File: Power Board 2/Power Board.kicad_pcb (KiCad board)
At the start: 4 copper layers, 191 parts, among them IC1 LTC4151IMS#PBF, IC2 LTC4151IMS#PBF, J1 Conn_01x02, J18 Conn_02x03_Top_Bottom, J19 Conn_01x02, J2 Conn_01x02, J21 Conn_01x02, J3 Conn_01x02, J4 Conn_01x02, J5 Conn_01x02, J6 Conn_01x02, J7 Conn_01x02, J8 Conn_01x02, J9 Conn_02x03_Top_Bottom, Q1 Q_PMOS_GDS, Q10 Q_NMOS_GDS, Q11 Q_NMOS_GDS, Q12 Q_NMOS_GDS, Q13 Q_NMOS_GDS, Q14 Q_NMOS_GDS, Q15 Q_NMOS_GDS, Q16 Q_NMOS_GDS, Q17 Q_NMOS_GDS, Q18 Q_NMOS_GDS, Q19 Q_NMOS_GDS, Q2 Q_PMOS_GDS, Q20 Q_NMOS_GDS, Q21 Q_NMOS_GDS, Q22 Q_NMOS_GDS, Q3 Q_PMOS_GDS, Q4 Q_PMOS_GDS, Q5 Q_PMOS_GDS, Q6 Q_PMOS_GDS, Q7 Q_PMOS_GDS, Q8 Q_PMOS_GDS, Q9 Q_NMOS_GDS, U1 LTC4372CDD-PBF, U10 ACS770xCB-050U-PFF, U11 ACS770xCB-050U-PFF, U12 ACS770xCB-050U-PFF, U13 ACS770xCB-050U-PFF, U14 ACS770xCB-050U-PFF, U15 ADC128S052CIMT, U17 TLV70033_SOT23-5, U2 LTC4372CDD-PBF, U3 LTC4372CDD-PBF, U4 LTC4372CDD-PBF, U5 LTC4372CDD-PBF, U6 LTC4372CDD-PBF, U7 LTC4372CDD-PBF, U8 ACS770xCB-050U-PFF, U9 ACS770xCB-050U-PFF

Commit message: added mounting holes
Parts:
- added H29: MountingHole_Pad, MountingHole:MountingHole_3.2mm_M3_DIN965, F.Cu at (149.5, 113.8)
- moved H5 0.08 mm to (52.9, 113.8)
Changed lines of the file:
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@@
 		(embedded_fonts no)
 	)
+	(footprint "MountingHole:MountingHole_3.2mm_M3_DIN965"
+		(layer "F.Cu")
+		(at 149.463953 113.821117)
+		(descr "Mounting Hole 3.2mm, M3, no annular, generated by kicad-footprint-generator mountinghole.py")
+		(tags "mountinghole M3 DIN965")
+		(property "Reference" "H29"
+			(at 3.425657 -2.784012 0)
+			(layer "F.SilkS")
+			(effects
+				(font
+					(size 1 1)
+					(thickness 0.15)
+				)
+			)
+		)
+		(property "Value" "MountingHole_Pad"
+			(at 0 3.75 0)
+			(layer "F.Fab")
+			(effects
+				(font
+					(size 1 1)
+					(thickness 0.15)
+				)
+			)
+		)
+		(property "Datasheet" "~"
+			(at 0 0 0)
+			(layer "F.Fab")
+			(hide yes)
+			(effects
+				(font
+					(size 1.27 1.27)
+					(thickness 0.15)
+				)
+			)
+		)
+		(property "Description" "Mounting Hole without connection"
+			(at 0 0 0)
+			(layer "F.Fab")
+			(hide yes)
+			(effects
+				(font
+					(size 1.27 1.27)
+					(thickness 0.15)
+				)
+			)
+		)
+		(attr exclude_from_pos_files exclude_from_bom)
+		(fp_circle
+			(center 0 0)
+			(end 2.8 0)
+			(stroke
+				(width 0.15)
+				(type solid)
+			)
+			(fill no)
+			(layer "Cmts.User")
+		)
+		(fp_circle
+			(center 0 0)
+			(end 3.05 0)
+			(stroke
+				(width 0.05)
+				(type solid)
+			)
+			(fill no)
+			(layer "F.CrtYd")
+		)
+		(fp_text user "${REFERENCE}"
+			(at 0 0 0)
+			(layer "F.Fab")
+			(effects
+				(font
+					(size 1 1)
+					(thickness 0.15)
+				)
+			)
+		)
+		(pad "" np_thru_hole circle
+			(at 0 0)
+			(size 3.2 3.2)
+			(drill 3.2)
+			(layers "*.Cu" "*.Mask")
+		)
+		(embedded_fonts no)
+	)
 	(footprint "Capacitor_SMD:C_0603_1608Metric"
 		(layer "F.Cu")
@@
 	(footprint "MountingHole:MountingHole_3.2mm_M3_DIN965"
 		(layer "F.Cu")
-		(at 52.785 113.821117)
+		(at 52.863953 113.821117)
 		(descr "Mounting Hole 3.2mm, M3, no annular, generated by kicad-footprint-generator mountinghole.py")
 		(tags "mountinghole M3 DIN965")

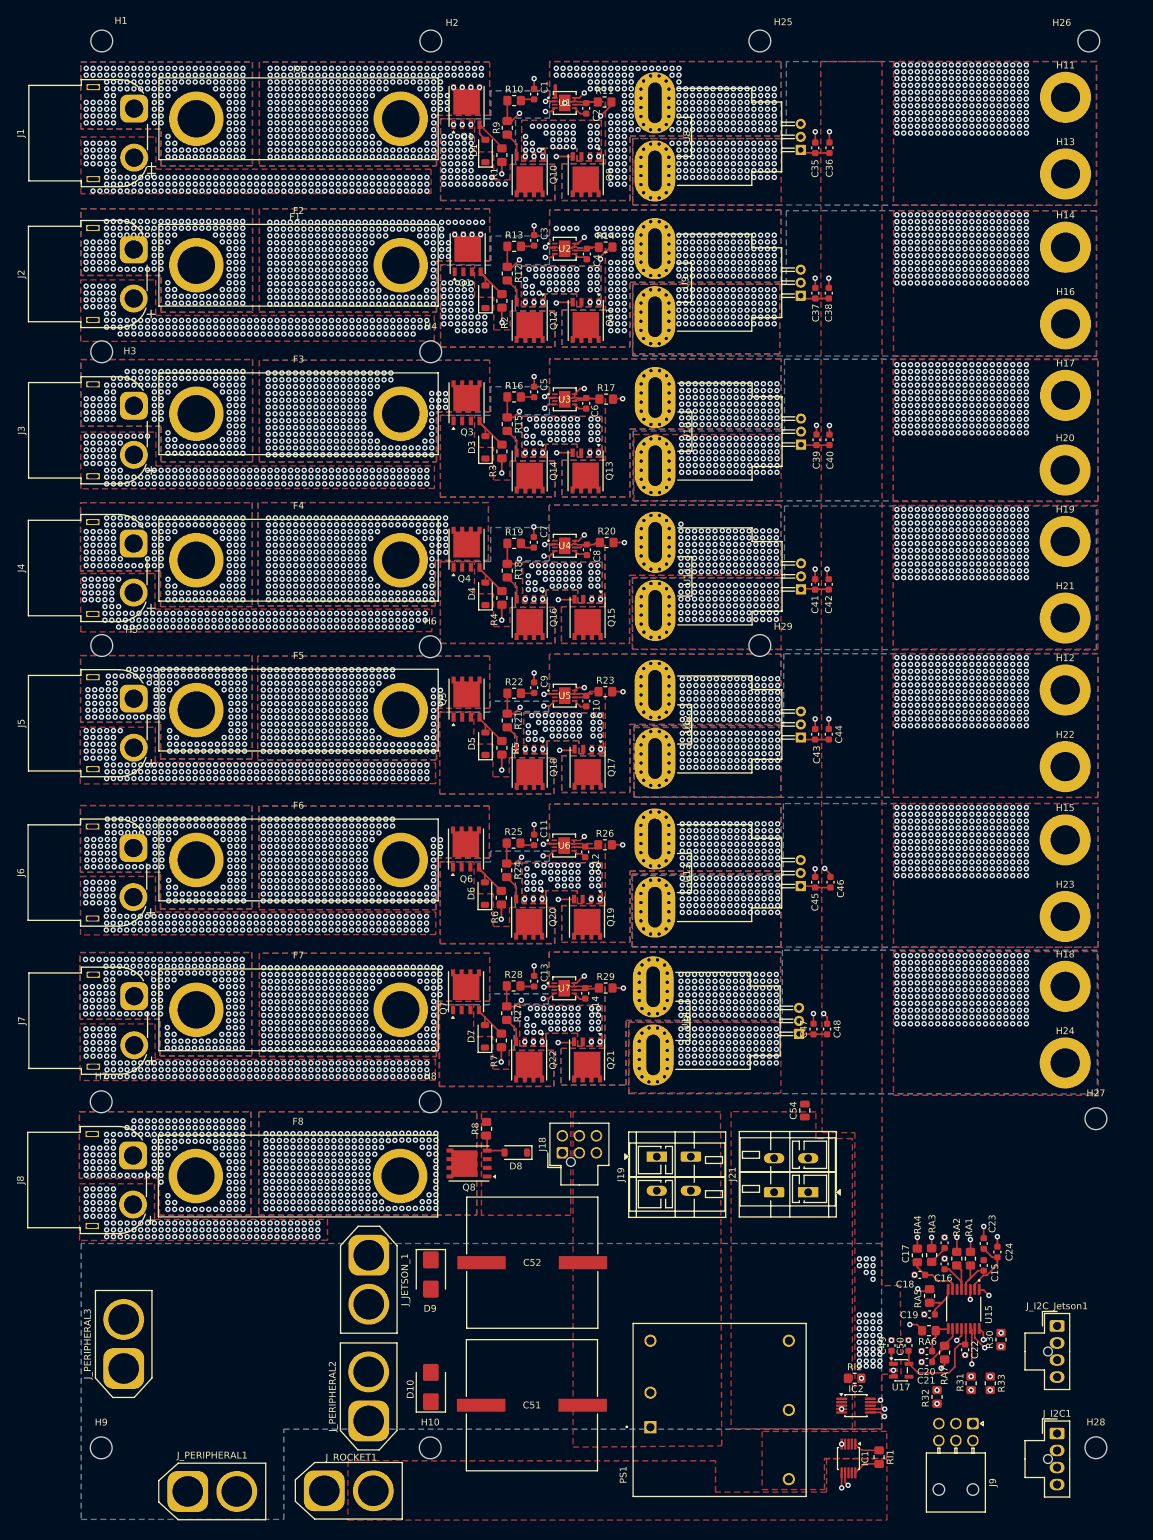
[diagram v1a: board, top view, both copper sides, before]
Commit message: minor updates to BMS; edge cuts, GND pour, via stitching, missed connections for PDB
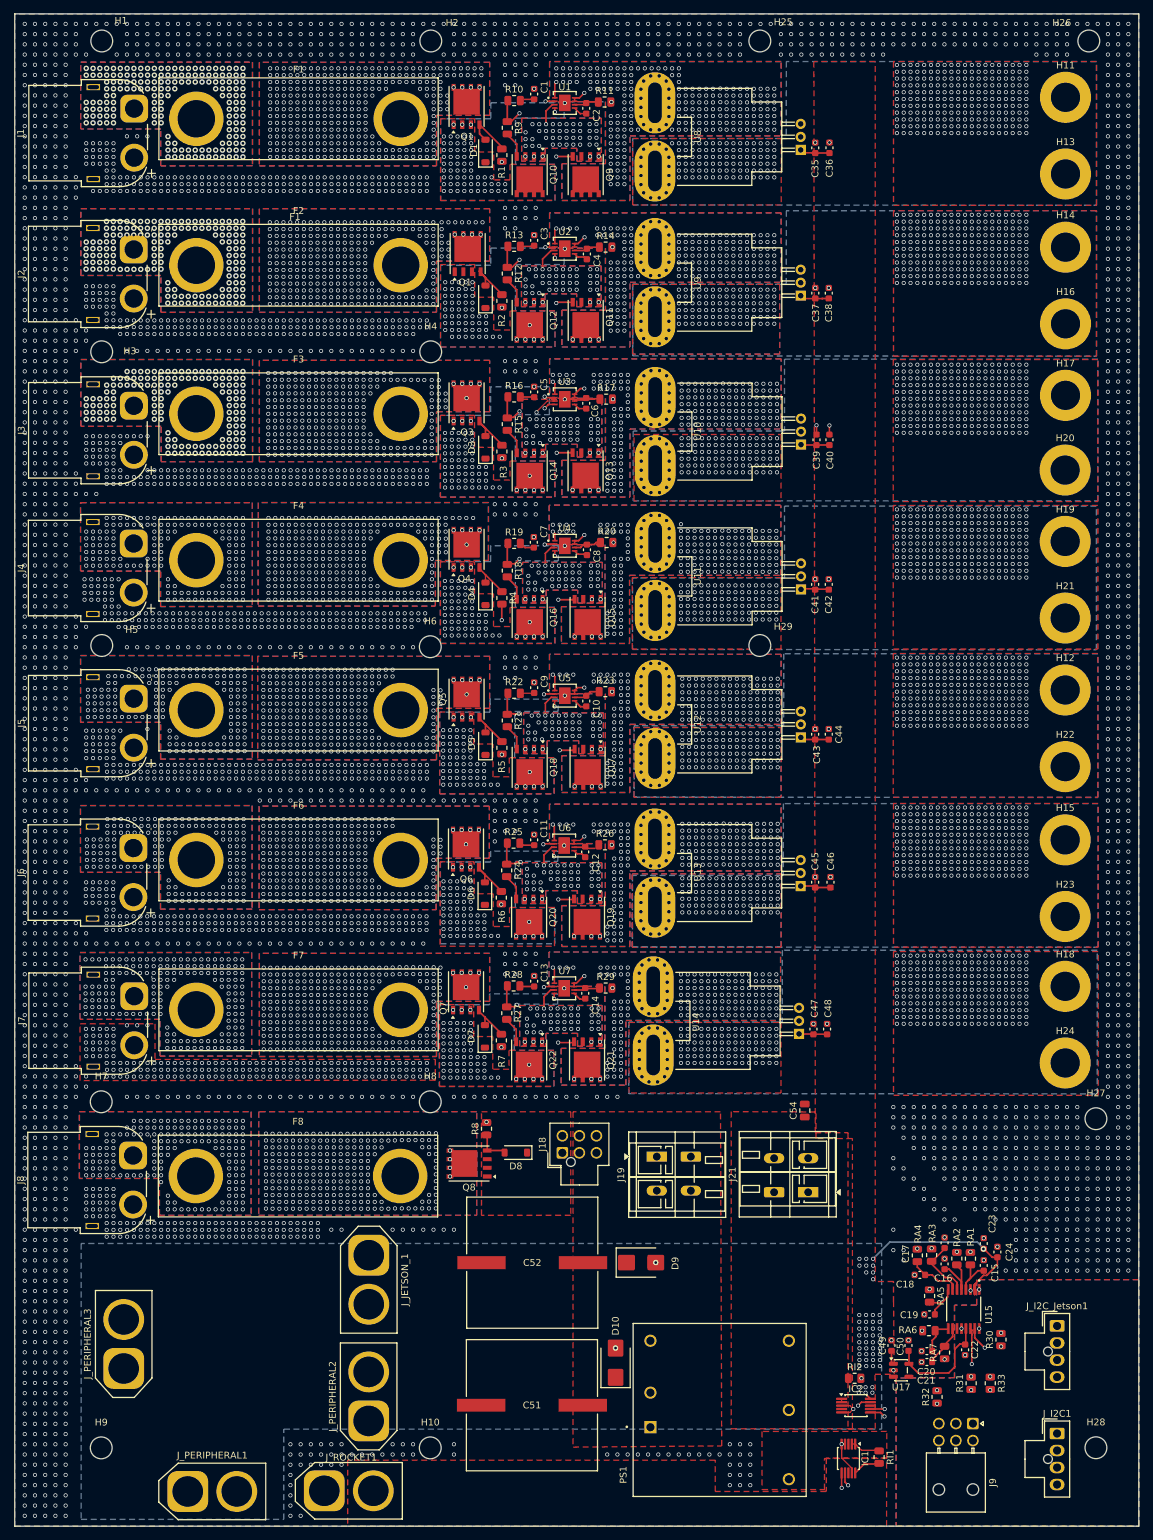
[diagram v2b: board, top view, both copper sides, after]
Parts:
- R1, R10, R11, R12, R13, R14, R15, R16, R17, R18, R19, R2, R20, R21, R22, R23, R24, R25, R26, R27, R28, R29, R3, R30, R31, R32, R33, R4, R5, R6, R7, R8, R9, RA1, RA2, RA3, RA4, RA5, RA6, RA7, RI1, RI2: footprint Resistor_SMD:R_0805_2012Metric_Pad1.20x1.40mm_HandSolder -> Resistor_SMD:R_0805_2012Metric
- moved D9 30.9 mm to (132.0, 204.4), turned to 0 degrees
- moved D10 27.3 mm to (128.3, 219.1)
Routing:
- net GND: track 68.4 -> 18.2 mm, vias 1343 -> 3455
- net /5V_REGULATED: track 41.0 -> 60.7 mm, vias 46 -> 53
- net Net-(U15-IN2): track 2.81 -> 9.09 mm
- net Net-(Q11-S): track 0.00 -> 3.84 mm, vias 48 -> 45
- net Net-(Q21-S): track 0.00 -> 3.67 mm
- net Net-(Q10-S): track 0.00 -> 3.63 mm, vias 39 -> 45
- net Net-(Q17-S): track 0.00 -> 3.57 mm
- net Net-(Q15-S): track 0.00 -> 3.57 mm
- net Net-(Q19-S): track 0.00 -> 3.52 mm
- net Net-(Q13-S): track 0.00 -> 3.43 mm, vias 42 -> 46
- net /BATT_5_PRESENSE: track 0.00 -> 2.45 mm, vias 105 -> 160
- net /BATT_6_PRESENSE: track 0.00 -> 2.42 mm, vias 105 -> 161
- net /BATT_7_PRESENSE: track 0.00 -> 2.38 mm, vias 105 -> 155
- net /BATT_2_PRESENSE: track 0.00 -> 2.31 mm, vias 164 -> 167
- net GNDD: track 2.10 -> 0.09 mm
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- added copper zone on B.Cu, net GND
- added copper zone on In2.Cu, net GND
- added copper zone on B.Cu, net GNDD
- added copper zone on F.Cu, net GNDD
- added copper zone on In2.Cu, net GNDD
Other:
- board outline added: 165 x 222 mm
- board text removed: "+"
- board text removed: "U9"
